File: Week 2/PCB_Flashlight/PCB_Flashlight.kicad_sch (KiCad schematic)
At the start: 18 parts, among them Q1 Q_NMOS_DSG, SW1 ON, SW2 BLINK, U2 MCP1799T-5002H/TT

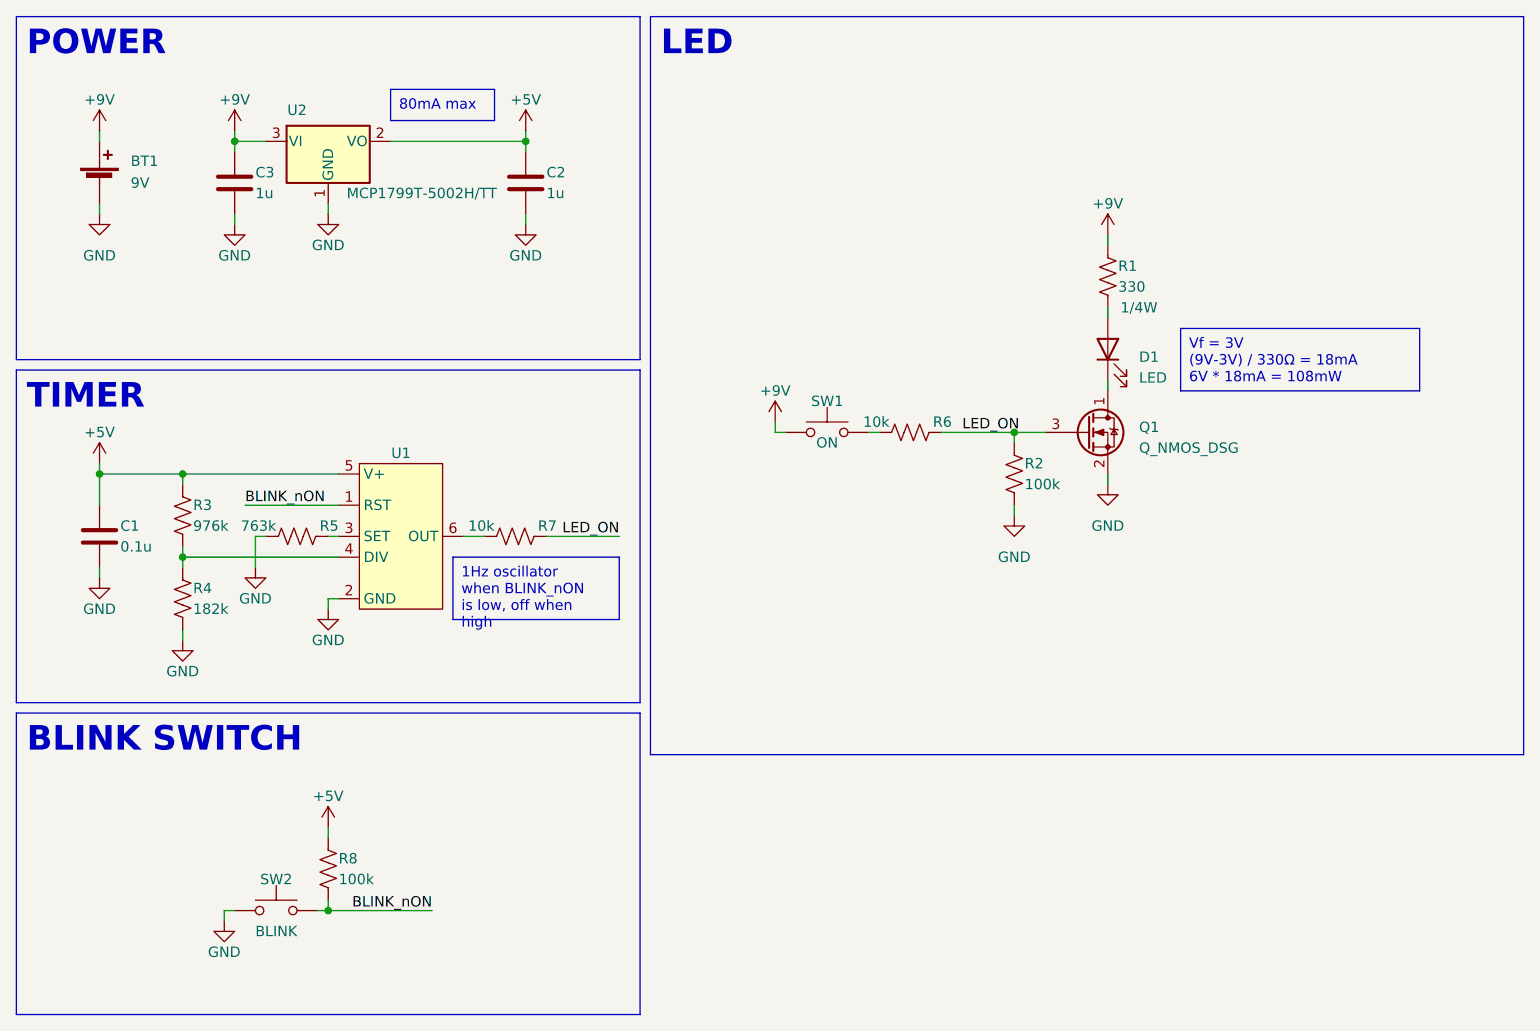
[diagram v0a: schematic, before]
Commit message: Rearrange, make workshop 2 content
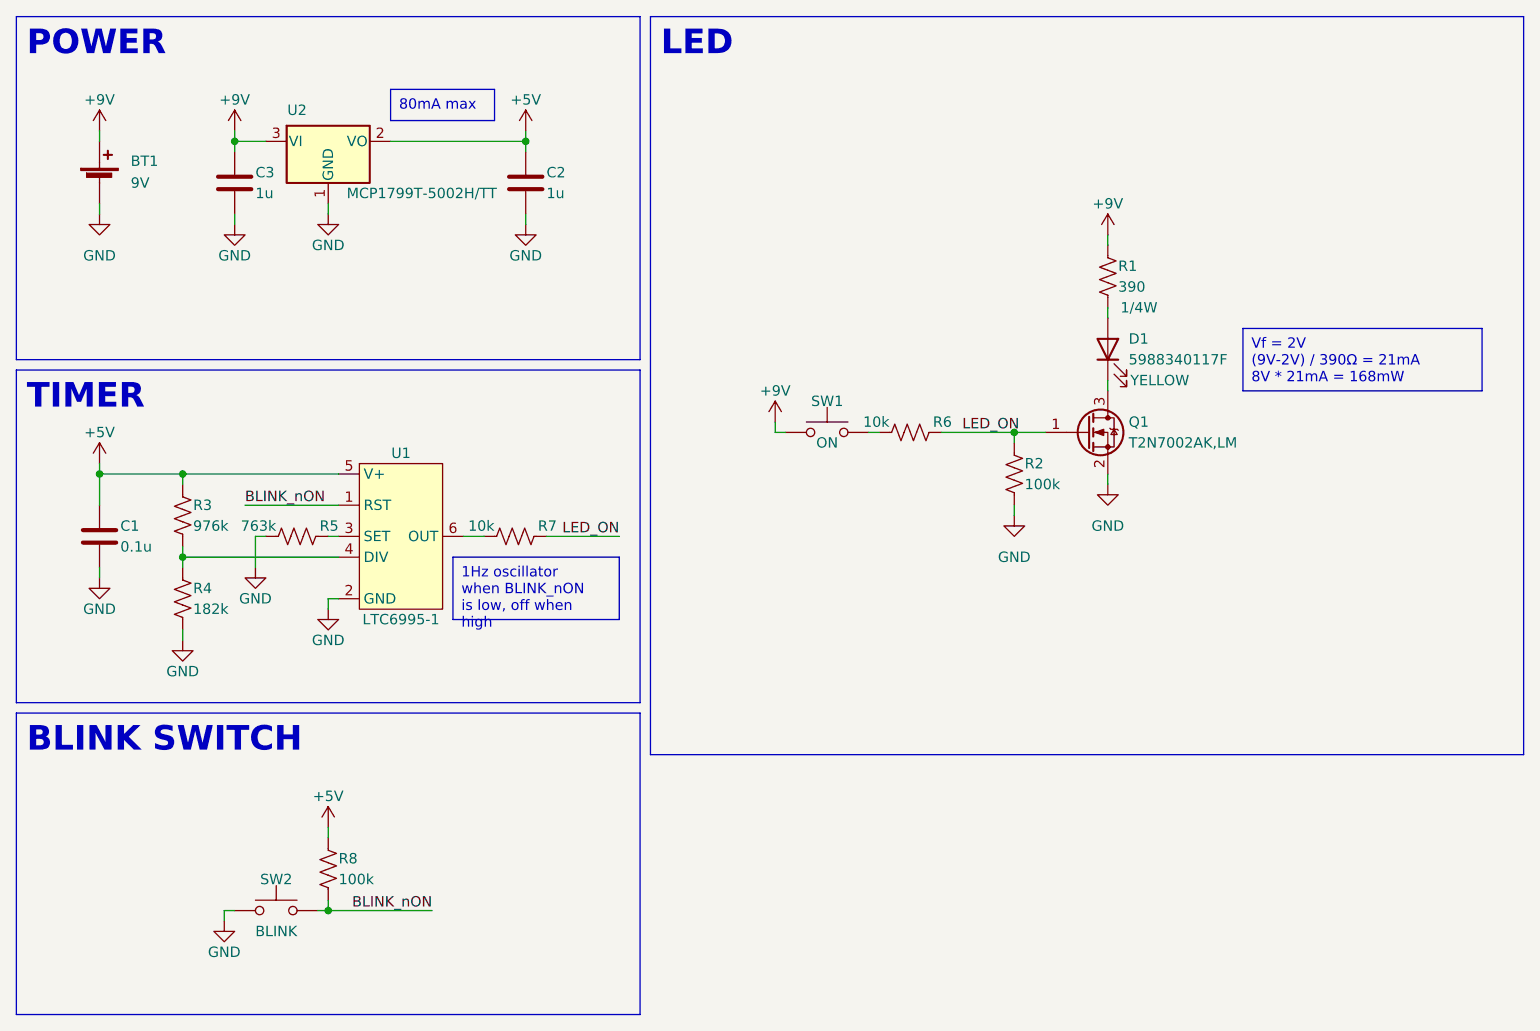
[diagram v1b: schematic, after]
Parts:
- BT1: footprint (none) -> Connector_PinHeader_2.54mm:PinHeader_1x02_P2.54mm_Vertical
- C1, C2, C3: footprint (none) -> Capacitor_SMD:C_0805_2012Metric_Pad1.18x1.45mm_HandSolder
- D1: value LED -> 5988340117F; footprint (none) -> FlashlightFootprints:5988340117F; Color (none) -> YELLOW
- Q1: value Q_NMOS_DSG -> T2N7002AK,LM; footprint (none) -> Package_TO_SOT_SMD:SOT-23_Handsoldering; symbol Device:Q_NMOS_DSG -> Device:Q_NMOS_GSD
- R1: value 330 -> 390; footprint (none) -> Resistor_SMD:R_0805_2012Metric_Pad1.20x1.40mm_HandSolder
- R2, R3, R4, R5, R6, R7, R8: footprint (none) -> Resistor_SMD:R_0805_2012Metric_Pad1.20x1.40mm_HandSolder
- SW1, SW2: footprint (none) -> Button_Switch_THT:SW_PUSH_6mm
- U1: value ~ -> LTC6995-1
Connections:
- net LED_ON: now also Q1.1 (G); no longer Q1.3 (G)
- net at D1.1 (K): now also Q1.3 (D); no longer Q1.1 (D)
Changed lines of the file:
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@@
     (effects (font (size 1.27 1.27) (color 0 0 0 1)) (justify left top))
   )
-  (text_box "Vf = 3V\n(9V-3V) / 330Ω = 18mA\n6V * 18mA = 108mW"
-    (at 154.94 50.8 0) (size 29.21 7.62)
+  (text_box "Vf = 2V\n(9V-2V) / 390Ω = 21mA\n8V * 21mA = 168mW"
+    (at 162.56 50.8 0) (size 29.21 7.62)
     (stroke (width 0) (type default) (color 0 0 0 1))
     (fill (type color) (color 255 255 194 1))
@@
     (effects (font (size 1.27 1.27)) (justify left bottom))
   )
-  (netclass_flag "" (length 2.54) (shape round) (at 146.05 49.53 90) (fields_autoplaced)
-    (effects (font (size 1.27 1.27) (color 255 0 0 1)) (justify left bottom))
-    (property "Netclass" "HIGHPOWER" (at 143.51 48.8315 90)
-      (effects (font (size 1.27 1.27) italic) (justify left))
-    )
-  )
   (symbol (lib_id "power:GND") (at 134.62 73.66 0) (unit 1)
     (in_bom yes) (on_board yes) (dnp no) (fields_autoplaced)
@@
       (effects (font (size 1.27 1.27)) (justify left))
     )
-    (property "Footprint" "" (at 51.816 117.094 90)
+    (property "Footprint" "Resistor_SMD:R_0805_2012Metric_Pad1.20x1.40mm_HandSolder" (at 51.816 117.094 90)
       (effects (font (size 1.27 1.27)) hide)
     )
@@
       (effects (font (size 1.27 1.27)) (justify left))
     )
-    (property "Footprint" "" (at 23.8252 80.01 0)
+    (property "Footprint" "Capacitor_SMD:C_0805_2012Metric_Pad1.18x1.45mm_HandSolder" (at 23.8252 80.01 0)
       (effects (font (size 1.27 1.27)) hide)
     )
@@
       (effects (font (size 1.27 1.27)) (justify left))
     )
-    (property "Footprint" "" (at 22.86 31.496 90)
+    (property "Footprint" "Connector_PinHeader_2.54mm:PinHeader_1x02_P2.54mm_Vertical" (at 22.86 31.496 90)
       (effects (font (size 1.27 1.27)) hide)
     )
@@
       (effects (font (size 1.27 1.27)) (justify left))
     )
-    (property "Value" "330" (at 147.32 45.72 0)
-      (effects (font (size 1.27 1.27)) (justify left))
-    )
-    (property "Footprint" "" (at 147.066 44.704 90)
+    (property "Value" "390" (at 147.32 45.72 0)
+      (effects (font (size 1.27 1.27)) (justify left))
+    )
+    (property "Footprint" "Resistor_SMD:R_0805_2012Metric_Pad1.20x1.40mm_HandSolder" (at 147.066 44.704 90)
       (effects (font (size 1.27 1.27)) hide)
     )
@@
     )
   )
-  (symbol (lib_id "Device:Q_NMOS_DSG") (at 143.51 63.5 0) (unit 1)
-    (in_bom yes) (on_board yes) (dnp no) (fields_autoplaced)
-    (property "Reference" "Q1" (at 149.86 62.865 0)
-      (effects (font (size 1.27 1.27)) (justify left))
-    )
-    (property "Value" "Q_NMOS_DSG" (at 149.86 65.405 0)
-      (effects (font (size 1.27 1.27)) (justify left))
-    )
-    (property "Footprint" "" (at 148.59 60.96 0)
-      (effects (font (size 1.27 1.27)) hide)
-    )
-    (property "Datasheet" "~" (at 143.51 63.5 0)
+  (symbol (lib_id "Device:Q_NMOS_GSD") (at 143.51 63.5 0) (unit 1)
+    (in_bom yes) (on_board yes) (dnp no)
+    (property "Reference" "Q1" (at 148.59 62.23 0)
+      (effects (font (size 1.27 1.27)) (justify left))
+    )
+    (property "Value" "T2N7002AK,LM" (at 148.59 64.77 0)
+      (effects (font (size 1.27 1.27)) (justify left))
+    )
+    (property "Footprint" "Package_TO_SOT_SMD:SOT-23_Handsoldering" (at 148.59 60.96 0)
+      (effects (font (size 1.27 1.27)) hide)
+    )
+    (property "Datasheet" "https://toshiba.semicon-storage.com/info/T2N7002AK_datasheet_en_20150401.pdf?did=29712&prodName=T2N7002AK" (at 143.51 63.5 0)
       (effects (font (size 1.27 1.27)) hide)
     )
@@
       (effects (font (size 1.27 1.27)) (justify left))
     )
-    (property "Footprint" "" (at 47.244 75.184 90)
+    (property "Footprint" "Resistor_SMD:R_0805_2012Metric_Pad1.20x1.40mm_HandSolder" (at 47.244 75.184 90)
       (effects (font (size 1.27 1.27)) hide)
     )
@@
       (effects (font (size 1.27 1.27)) (justify left))
     )
-    (property "Footprint" "" (at 40.3352 36.83 0)
+    (property "Footprint" "Capacitor_SMD:C_0805_2012Metric_Pad1.18x1.45mm_HandSolder" (at 40.3352 36.83 0)
       (effects (font (size 1.27 1.27)) hide)
     )
@@
   )
   (symbol (lib_id "FlashlightLib:LTC6995-1") (at 59.69 76.2 0) (unit 1)
-    (in_bom yes) (on_board yes) (dnp no) (fields_autoplaced)
+    (in_bom yes) (on_board yes) (dnp no)
     (property "Reference" "U1" (at 59.69 66.04 0)
       (effects (font (size 1.27 1.27)))
     )
-    (property "Value" "~" (at 57.15 78.74 0)
+    (property "Value" "LTC6995-1" (at 59.69 86.36 0)
       (effects (font (size 1.27 1.27)))
     )
@@
   )
   (symbol (lib_id "Device:LED") (at 146.05 53.34 90) (unit 1)
-    (in_bom yes) (on_board yes) (dnp no) (fields_autoplaced)
-    (property "Reference" "D1" (at 149.86 54.2925 90)
+    (in_bom yes) (on_board yes) (dnp no)
+    (property "Reference" "D1" (at 148.59 52.07 90)
       (effects (font (size 1.27 1.27)) (justify right))
     )
-    (property "Value" "LED" (at 149.86 56.8325 90)
+    (property "Value" "5988340117F" (at 148.59 54.61 90)
       (effects (font (size 1.27 1.27)) (justify right))
     )
-    (property "Footprint" "" (at 146.05 53.34 0)
-      (effects (font (size 1.27 1.27)) hide)
-    )
-    (property "Datasheet" "~" (at 146.05 53.34 0)
-      (effects (font (size 1.27 1.27)) hide)
+    (property "Footprint" "FlashlightFootprints:5988340117F" (at 146.05 53.34 0)
+      (effects (font (size 1.27 1.27)) hide)
+    )
+    (property "Datasheet" "https://s3-us-west-2.amazonaws.com/catsy.557/Dialight_CBI_data_598-singleRA-1208_Mar2019.pdf" (at 146.05 53.34 0)
+      (effects (font (size 1.27 1.27)) hide)
+    )
+    (property "Color" "YELLOW" (at 152.4 57.15 90)
+      (effects (font (size 1.27 1.27)))
     )
     (pin "1")
@@
       (effects (font (size 1.27 1.27)) (justify left))
     )
-    (property "Footprint" "" (at 34.036 84.074 90)
+    (property "Footprint" "Resistor_SMD:R_0805_2012Metric_Pad1.20x1.40mm_HandSolder" (at 34.036 84.074 90)
       (effects (font (size 1.27 1.27)) hide)
     )
@@
       (effects (font (size 1.27 1.27)) (justify left))
     )
-    (property "Footprint" "" (at 75.8952 36.83 0)
+    (property "Footprint" "Capacitor_SMD:C_0805_2012Metric_Pad1.18x1.45mm_HandSolder" (at 75.8952 36.83 0)
       (effects (font (size 1.27 1.27)) hide)
     )
@@
       (effects (font (size 1.27 1.27)))
     )
-    (property "Footprint" "" (at 111.76 58.42 0)
+    (property "Footprint" "Button_Switch_THT:SW_PUSH_6mm" (at 111.76 58.42 0)
       (effects (font (size 1.27 1.27)) hide)
     )
@@
       (effects (font (size 1.27 1.27)))
     )
-    (property "Footprint" "" (at 44.45 116.84 0)
+    (property "Footprint" "Button_Switch_THT:SW_PUSH_6mm" (at 44.45 116.84 0)
       (effects (font (size 1.27 1.27)) hide)
     )
@@
       (effects (font (size 1.27 1.27)) (justify left))
     )
-    (property "Footprint" "" (at 135.636 68.834 90)
+    (property "Footprint" "Resistor_SMD:R_0805_2012Metric_Pad1.20x1.40mm_HandSolder" (at 135.636 68.834 90)
       (effects (font (size 1.27 1.27)) hide)
     )
@@
       (effects (font (size 1.27 1.27)) (justify left))
     )
-    (property "Footprint" "" (at 73.914 75.184 90)
+    (property "Footprint" "Resistor_SMD:R_0805_2012Metric_Pad1.20x1.40mm_HandSolder" (at 73.914 75.184 90)
       (effects (font (size 1.27 1.27)) hide)
     )
@@
       (effects (font (size 1.27 1.27)) (justify left))
     )
-    (property "Footprint" "" (at 122.174 62.484 90)
+    (property "Footprint" "Resistor_SMD:R_0805_2012Metric_Pad1.20x1.40mm_HandSolder" (at 122.174 62.484 90)
       (effects (font (size 1.27 1.27)) hide)
     )
@@
       (effects (font (size 1.27 1.27)) (justify left))
     )
-    (property "Footprint" "" (at 34.036 73.914 90)
-      (effects (font (size 1.27 1.27)) hide)
-    )
+    (property "Footprint" "Resistor_SMD:R_0805_2012Metric_Pad1.20x1.40mm_HandSolder" (at 34.036 73.914 90)
+      (effects (font (size 1.27 1.27)) hide)
+    )
